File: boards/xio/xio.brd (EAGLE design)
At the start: 170 x 100 mm, 146 parts, among them Y2 NX3225SA-12.000MHZ-STD-CSR-1

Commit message: Latest snapshot
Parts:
- removed C36, C51: 0.1uF, rcl:C0402K
- removed ECI: eci, microbuilder:2X23
- removed XIO: STM32H753B-XIO, sjg-stm32:PQFP208
- added JP1: (no value), pinhead:1X04
- added JP2, JP3: (no value), pinhead:2X06
- added TP1, TP2, TP3, TP4: (no value), microbuilder:TESTPOINT_ROUND_1MM
- added U$2: A8_CART, sjg-con:A8_CART
- added U$3: XIO, sjg-stm32:PQFP208
- moved ARCH_ID 147.5 mm to (152.6, 92.3), turned to 0 degrees
- moved R6 142.0 mm to (156.6, 85.9)
- moved R7 139.9 mm to (154.0, 85.9)
- moved PID 139.0 mm to (140.0, 92.5), turned to 0 degrees
- moved R8 137.9 mm to (151.5, 85.9)
- moved R9 135.9 mm to (149.0, 85.9)
- moved MEM_ID 133.5 mm to (129.9, 92.7), turned to 0 degrees
- moved R14 131.3 mm to (142.4, 86.0)
- moved R15 129.6 mm to (139.9, 86.0)
- moved R16 127.9 mm to (137.3, 86.0)
- moved R17 125.3 mm to (132.1, 86.1)
- moved R18 122.8 mm to (128.3, 86.1)
- moved C35 96.3 mm to (142.6, 15.2), turned to 180 degrees
- moved XIO-SWD 69.2 mm to (4.11, 26.5), turned to 270 degrees
- moved R89 64.2 mm to (8.68, 25.4), turned to 270 degrees
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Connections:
- removed net I2C_SCL: SLOT0.B42, SLOT1.B42, SLOT2.B42, SLOT3.B42, SLOT4.B42, XIO.91
- removed net I2C_SDA: SLOT0.B43, SLOT1.B43, SLOT2.B43, SLOT3.B43, SLOT4.B43, XIO.90
- new net AUX_CTS: JP1.1, SLOT0.B46, SLOT1.B46, SLOT2.B46, SLOT3.B46, SLOT4.B46, U$3.30
- new net AUX_RTS: JP1.4, SLOT0.B47, SLOT1.B47, SLOT2.B47, SLOT3.B47, SLOT4.B47, U$3.29
- new net AUX_RX: JP1.2, SLOT0.B48, SLOT1.B48, SLOT2.B48, SLOT3.B48, SLOT4.B48, U$3.27
- new net AUX_TX: JP1.3, SLOT0.B49, SLOT1.B49, SLOT2.B49, SLOT3.B49, SLOT4.B49, U$3.28
- new net N$3: TP1.P$1, U$3.134
- new net N$4: TP2.P$1, U$3.178
- new net N$5: TP3.P$1, U$3.102
- new net N$6: TP4.P$1, U$3.175
- new net USRA_CLK: JP2.1, U$3.45
- new net USRA_D0: JP2.3, U$3.35
- new net USRA_D1: JP2.4, U$3.36
- new net USRA_D2: JP2.5, U$3.37
- new net USRA_D3: JP2.6, U$3.38
- new net USRA_D4: JP2.7, U$3.57
- new net USRA_D5: JP2.8, U$3.58
- new net USRA_D6: JP2.9, U$3.138
- new net USRA_D7: JP2.10, U$3.139
- new net USRA_MISC: JP2.11, U$3.10
- new net USRB_CLK: JP3.1, U$3.130
- new net USRB_D0: JP3.3, U$3.126
- new net USRB_D1: JP3.4, U$3.127
- new net USRB_D2: JP3.5, U$3.128
- new net USRB_D3: JP3.6, U$3.186
- new net USRB_D4: JP3.7, U$3.187
- new net USRB_D5: JP3.8, U$3.188
- new net USRB_D6: JP3.9, U$3.189
- new net USRB_D7: JP3.10, U$3.190
- new net USRB_MISC: JP3.11, U$3.177
- net !RESET!: now also U$3.34; no longer XIO.34
- net !VHDCI_EXSEL!: now also U$3.68; no longer ECI.1, XIO.68
- net !VHDCI_IRQ!: now also U$3.69; no longer ECI.2, XIO.69
- net !VHDCI_MPD!: now also U$3.67; no longer ECI.3, XIO.67
- net +3V3: now also JP2.2, JP3.2, U$3.103, U$3.115, U$3.124, U$3.137, U$3.15, U$3.150, U$3.158, U$3.171, U$3.185, U$3.204, U$3.26, U$3.39, U$3.52, U$3.59, U$3.6, U$3.73, U$3.83, U$3.94; no longer XIO.103, XIO.115, XIO.124, XIO.137, XIO.15, XIO.150, XIO.158, XIO.171, XIO.185, XIO.204, XIO.26, XIO.39, XIO.52, XIO.59, XIO.6, XIO.73, XIO.83, XIO.94
- net +5V: now also U$2.P13; no longer C36.1, C51.1, ECI.42, ECI.44, ECI.46
- net ARCH0: now also U$3.96
- net ARCH1: now also U$3.97
- net ARCH2: now also U$3.98
- net ARCH3: now also U$3.99
- net A_OK: now also U$3.176
- net GND: now also JP2.12, JP3.12, U$2.PB, U$3.114, U$3.125, U$3.136, U$3.14, U$3.149, U$3.170, U$3.184, U$3.202, U$3.25, U$3.40, U$3.51, U$3.60, U$3.72, U$3.82, U$3.93; no longer C36.2, C51.2, ECI.41, ECI.43, ECI.45, SLOT0.B41, SLOT0.B44, SLOT1.B41, SLOT1.B44, SLOT2.B41, SLOT2.B44, SLOT3.B41, SLOT3.B44, SLOT4.B41, SLOT4.B44, XIO.114, XIO.125, XIO.136, XIO.14, XIO.149, XIO.170, XIO.184, XIO.202, XIO.25, XIO.40, XIO.51, XIO.60, XIO.72, XIO.82, XIO.93
- net MEM0: now also U$3.100
- net MEM1: now also U$3.101
- net N$1: now also U$3.33; no longer XIO.33
- net N$107: now also U$3.9; no longer XIO.192
- net N$108: now also U$3.111; no longer XIO.193
- net N$109: now also U$3.112; no longer XIO.104
- net N$11: now also U$3.197; no longer XIO.197
- net N$110: now also U$3.113; no longer XIO.31
- net N$111: now also U$3.31; no longer XIO.179
- net N$112: now also U$3.133; no longer XIO.180
- net N$13: now also U$3.46; no longer XIO.169
- net N$14: now also U$3.47; no longer XIO.172
- net N$15: now also U$3.48; no longer XIO.173
- net N$2: now also U$3.32; no longer XIO.32
- net N$34: now also U$3.167; no longer XIO.43
- net N$35: now also U$3.172; no longer XIO.50
- net N$39: now also U$3.169; no longer XIO.45
- net N$40: now also U$3.168; no longer XIO.44
- net N$57: now also U$3.54; no longer XIO.105
- net N$61: now also U$3.56; no longer XIO.107
- net N$64: now also U$3.160; no longer XIO.160
- net N$65: now also U$3.53; no longer XIO.199
- net N$7: now also U$3.203; no longer XIO.203
- net N$86: now also U$3.50; no longer XIO.61
- net N$93: now also U$3.8; no longer XIO.63
- net PID0: now also U$3.151
- net PID1: now also U$3.152
- net PID2: now also U$3.153
- net SD0: now also U$3.140
- net SD1: now also U$3.141
- net SD2: now also U$3.161
- net SD3: now also U$3.162
- net SDCD: now also U$3.173
- net SDCLK: now also U$3.163
- net SDCMD: now also U$3.166
- net SPI_CLK: now also SLOT0.B41, SLOT1.B41, SLOT2.B41, SLOT3.B41, SLOT4.B41; no longer SLOT0.B45, SLOT1.B45, SLOT2.B45, SLOT3.B45, SLOT4.B45
- net SPI_IRQ0: now also SLOT0.B42, U$3.179; no longer SLOT0.B48, XIO.99
- net SPI_IRQ1: now also SLOT1.B42, U$3.180; no longer SLOT1.B48, XIO.100
- net SPI_IRQ2: now also SLOT2.B42, U$3.181; no longer SLOT2.B48, XIO.101
- net SPI_IRQ3: now also SLOT3.B42, U$3.182; no longer SLOT3.B48, XIO.102
- net SPI_IRQ4: now also SLOT4.B42, U$3.183; no longer SLOT4.B48
- net SPI_MISO: now also SLOT0.B43, SLOT1.B43, SLOT2.B43, SLOT3.B43, SLOT4.B43, U$3.55; no longer SLOT0.B46, SLOT1.B46, SLOT2.B46, SLOT3.B46, SLOT4.B46, XIO.106
- net SPI_MOSI: now also SLOT0.B44, SLOT1.B44, SLOT2.B44, SLOT3.B44, SLOT4.B44; no longer SLOT0.B47, SLOT1.B47, SLOT2.B47, SLOT3.B47, SLOT4.B47
- net SPI_SS0: now also SLOT0.B45, U$3.1; no longer SLOT0.B49, XIO.46
- net SPI_SS1: now also SLOT1.B45, U$3.2; no longer SLOT1.B49, XIO.47
- net SPI_SS2: now also SLOT2.B45, U$3.3; no longer SLOT2.B49, XIO.48
- net SPI_SS3: now also SLOT3.B45, U$3.4; no longer SLOT3.B49, XIO.130
- net SPI_SS4: now also SLOT4.B45, U$3.5; no longer SLOT4.B49, XIO.96
- net VHDCI_A0: now also U$2.P5, U$3.107; no longer ECI.5, XIO.35
- net VHDCI_A1: now also U$2.P4, U$3.106; no longer ECI.6, XIO.36
- net VHDCI_A10: now also U$2.PP, U$3.194; no longer ECI.15, XIO.161
- net VHDCI_A11: now also U$2.PN, U$3.193; no longer ECI.16, XIO.162
- net VHDCI_A12: now also U$2.PK, U$3.192; no longer ECI.17, XIO.163
- net VHDCI_A13: now also U$3.63; no longer ECI.18, XIO.8
- net VHDCI_A14: now also U$3.62; no longer ECI.19, XIO.9
- net VHDCI_A15: now also U$3.61; no longer ECI.20, XIO.10
- net VHDCI_A2: now also U$2.P3, U$3.105; no longer ECI.7, XIO.37
- net VHDCI_A3: now also U$2.P2, U$3.104; no longer ECI.8, XIO.38
- net VHDCI_A4: now also U$2.PC, U$3.91; no longer ECI.9, XIO.57
- net VHDCI_A5: now also U$2.PD, U$3.90; no longer ECI.10, XIO.58
- net VHDCI_A6: now also U$2.PE, U$3.199; no longer ECI.11, XIO.138
- net VHDCI_A7: now also U$2.PF, U$3.198; no longer ECI.12, XIO.139
- net VHDCI_A8: now also U$2.PH, U$3.196; no longer ECI.13, XIO.140
- net VHDCI_A9: now also U$2.PJ, U$3.195; no longer ECI.14, XIO.141
- net VHDCI_AUDIO_SIO: no longer ECI.4
- net VHDCI_CCTL: now also U$2.P15, U$3.95; no longer ECI.21, XIO.95
- net VHDCI_CLK: now also U$2.PS, U$3.65; no longer ECI.22, XIO.65
- net VHDCI_D0: now also U$2.P10, U$3.154; no longer ECI.24, XIO.154
- net VHDCI_D1: now also U$2.P9, U$3.155; no longer ECI.25, XIO.155
- net VHDCI_D1XX: now also U$3.121; no longer ECI.23, XIO.121
- net VHDCI_D2: now also U$2.P8, U$3.156; no longer ECI.26, XIO.156
- net VHDCI_D3: now also U$2.PL, U$3.157; no longer ECI.27, XIO.157
- net VHDCI_D4: now also U$2.P6, U$3.205; no longer ECI.28, XIO.205
- net VHDCI_D5: now also U$2.P7, U$3.206; no longer ECI.29, XIO.206
- net VHDCI_D6: now also U$2.P11, U$3.207; no longer ECI.30, XIO.207
- net VHDCI_D7: now also U$2.PM, U$3.208; no longer ECI.31, XIO.208
- net VHDCI_GND: no longer ECI.32
- net VHDCI_HALT: now also U$3.123; no longer ECI.33, XIO.123
- net VHDCI_RD4: now also U$2.PA, U$3.66; no longer ECI.34, XIO.66
- net VHDCI_RD5: now also U$2.P14, U$3.64; no longer ECI.35, XIO.64
- net VHDCI_REF: now also U$3.120; no longer ECI.36, XIO.120
- net VHDCI_RSRVD0: now also U$3.7; no longer XIO.7
- net VHDCI_RSRVD1: now also U$3.11; no longer XIO.11
- net VHDCI_RSRVD2: now also U$3.12; no longer XIO.12
- net VHDCI_RSRVD3: now also U$3.13; no longer XIO.13
- net VHDCI_RSRVD4: now also U$3.19; no longer XIO.19
- net VHDCI_RSRVD5: now also U$3.20; no longer XIO.20
- net VHDCI_RSRVD6: now also U$3.21; no longer XIO.21
- net VHDCI_RST: now also U$3.122; no longer ECI.37, XIO.122
- net VHDCI_RW: now also U$2.PR, U$3.174; no longer ECI.38, XIO.174
- net VHDCI_S4: now also U$2.P1, U$3.119; no longer ECI.39, XIO.119
- net VHDCI_S5: now also U$2.P12, U$3.118; no longer ECI.40, XIO.118
- net XIO_RAM_A0: now also U$3.16; no longer XIO.16
- net XIO_RAM_A1: now also U$3.17; no longer XIO.17
- net XIO_RAM_A10: now also U$3.77; no longer XIO.77
- net XIO_RAM_A11: now also U$3.78; no longer XIO.78
- net XIO_RAM_A12: now also U$3.129; no longer XIO.129
- net XIO_RAM_A2: now also U$3.18; no longer XIO.18
- net XIO_RAM_A3: now also U$3.22; no longer XIO.22
- net XIO_RAM_A4: now also U$3.23; no longer XIO.23
- net XIO_RAM_A5: now also U$3.24; no longer XIO.24
- net XIO_RAM_A6: now also U$3.71; no longer XIO.71
- net XIO_RAM_A7: now also U$3.74; no longer XIO.74
- net XIO_RAM_A8: now also U$3.75; no longer XIO.75
- net XIO_RAM_A9: now also U$3.76; no longer XIO.76
- net XIO_RAM_BA0: now also U$3.131; no longer XIO.131
- net XIO_RAM_BA1: now also U$3.132; no longer XIO.132
- net XIO_RAM_CAS: now also U$3.191; no longer XIO.191
- net XIO_RAM_CLK: now also U$3.135; no longer XIO.135
- net XIO_RAM_D0: now also U$3.116; no longer XIO.116
- net XIO_RAM_D1: now also U$3.117; no longer XIO.117
- net XIO_RAM_D10: now also U$3.87; no longer XIO.87
- net XIO_RAM_D11: now also U$3.88; no longer XIO.88
- net XIO_RAM_D12: now also U$3.89; no longer XIO.89
- net XIO_RAM_D13: now also U$3.108; no longer XIO.108
- net XIO_RAM_D14: now also U$3.109; no longer XIO.109
- net XIO_RAM_D15: now also U$3.110; no longer XIO.110
- net XIO_RAM_D2: now also U$3.164; no longer XIO.164
- net XIO_RAM_D3: now also U$3.165; no longer XIO.165
- net XIO_RAM_D4: now also U$3.79; no longer XIO.79
- net XIO_RAM_D5: now also U$3.80; no longer XIO.80
- net XIO_RAM_D6: now also U$3.81; no longer XIO.81
- net XIO_RAM_D7: now also U$3.84; no longer XIO.84
- net XIO_RAM_D8: now also U$3.85; no longer XIO.85
- net XIO_RAM_D9: now also U$3.86; no longer XIO.86
- net XIO_RAM_DQMH: now also U$3.201; no longer XIO.201
- net XIO_RAM_DQML: now also U$3.200; no longer XIO.200
- net XIO_RAM_RAS: now also U$3.70; no longer XIO.70
- net XIO_RAM_WE: now also U$3.49; no longer XIO.49
- net XIO_RX: now also U$3.44; no longer XIO.196
- net XIO_SWDCLK: now also U$3.159; no longer XIO.159
- net XIO_SWDIO: now also U$3.147; no longer XIO.147
- net XIO_TX: now also U$3.43; no longer XIO.195
- net XIO_USB_N: now also U$3.145; no longer XIO.145
- net XIO_USB_P: now also U$3.146; no longer XIO.146
- net XIO_VCAP1: now also U$3.92; no longer XIO.92
- net XIO_VCAP2: now also U$3.148; no longer XIO.148
- net XIO_VDDA: now also U$3.41, U$3.42; no longer XIO.41, XIO.42
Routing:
- net GND: track 0.00 -> 467.5 mm, vias 0 -> 33
- net VHDCI_RW: track 0.00 -> 402.0 mm, vias 0 -> 13
- net VHDCI_S5: track 0.00 -> 388.4 mm, vias 0 -> 13
- net +5V: track 0.00 -> 369.2 mm, vias 0 -> 64
- net VHDCI_D4: track 0.00 -> 342.4 mm, vias 0 -> 10
- net VHDCI_D3: track 0.00 -> 331.5 mm, vias 0 -> 5
- net VHDCI_RD5: track 0.00 -> 325.1 mm, vias 0 -> 8
- net VHDCI_REF: track 0.00 -> 315.5 mm, vias 0 -> 12
- net ARCH2: track 0.00 -> 311.7 mm, vias 0 -> 8
- net VHDCI_D1: track 0.00 -> 309.7 mm, vias 0 -> 7
- net VHDCI_A7: track 0.00 -> 296.4 mm, vias 0 -> 11
- net VHDCI_S4: track 0.00 -> 294.4 mm, vias 0 -> 10
- net VHDCI_CLK: track 0.00 -> 290.0 mm, vias 0 -> 11
- net VHDCI_D0: track 0.00 -> 287.8 mm, vias 0 -> 8
- net VHDCI_D2: track 0.00 -> 287.3 mm, vias 0 -> 9
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- added copper zone on layer 15, net +3V3
- added copper zone on layer 15, net +5V
- added copper zone on layer 2, net GND
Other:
- board text added: "Indent SD card slot Make parts for STM32F Neaten everything up Add 5v plane rectangle Add GND plane Add 3.3v plane"
- board text removed: "Indent SD card slot Make parts for STM32F Neaten everything up Make cartridge part 5650118-1 and place Add 5v plane rectangle Add GND plane Add 3.3v plane Find better (larger) USB ESD part"

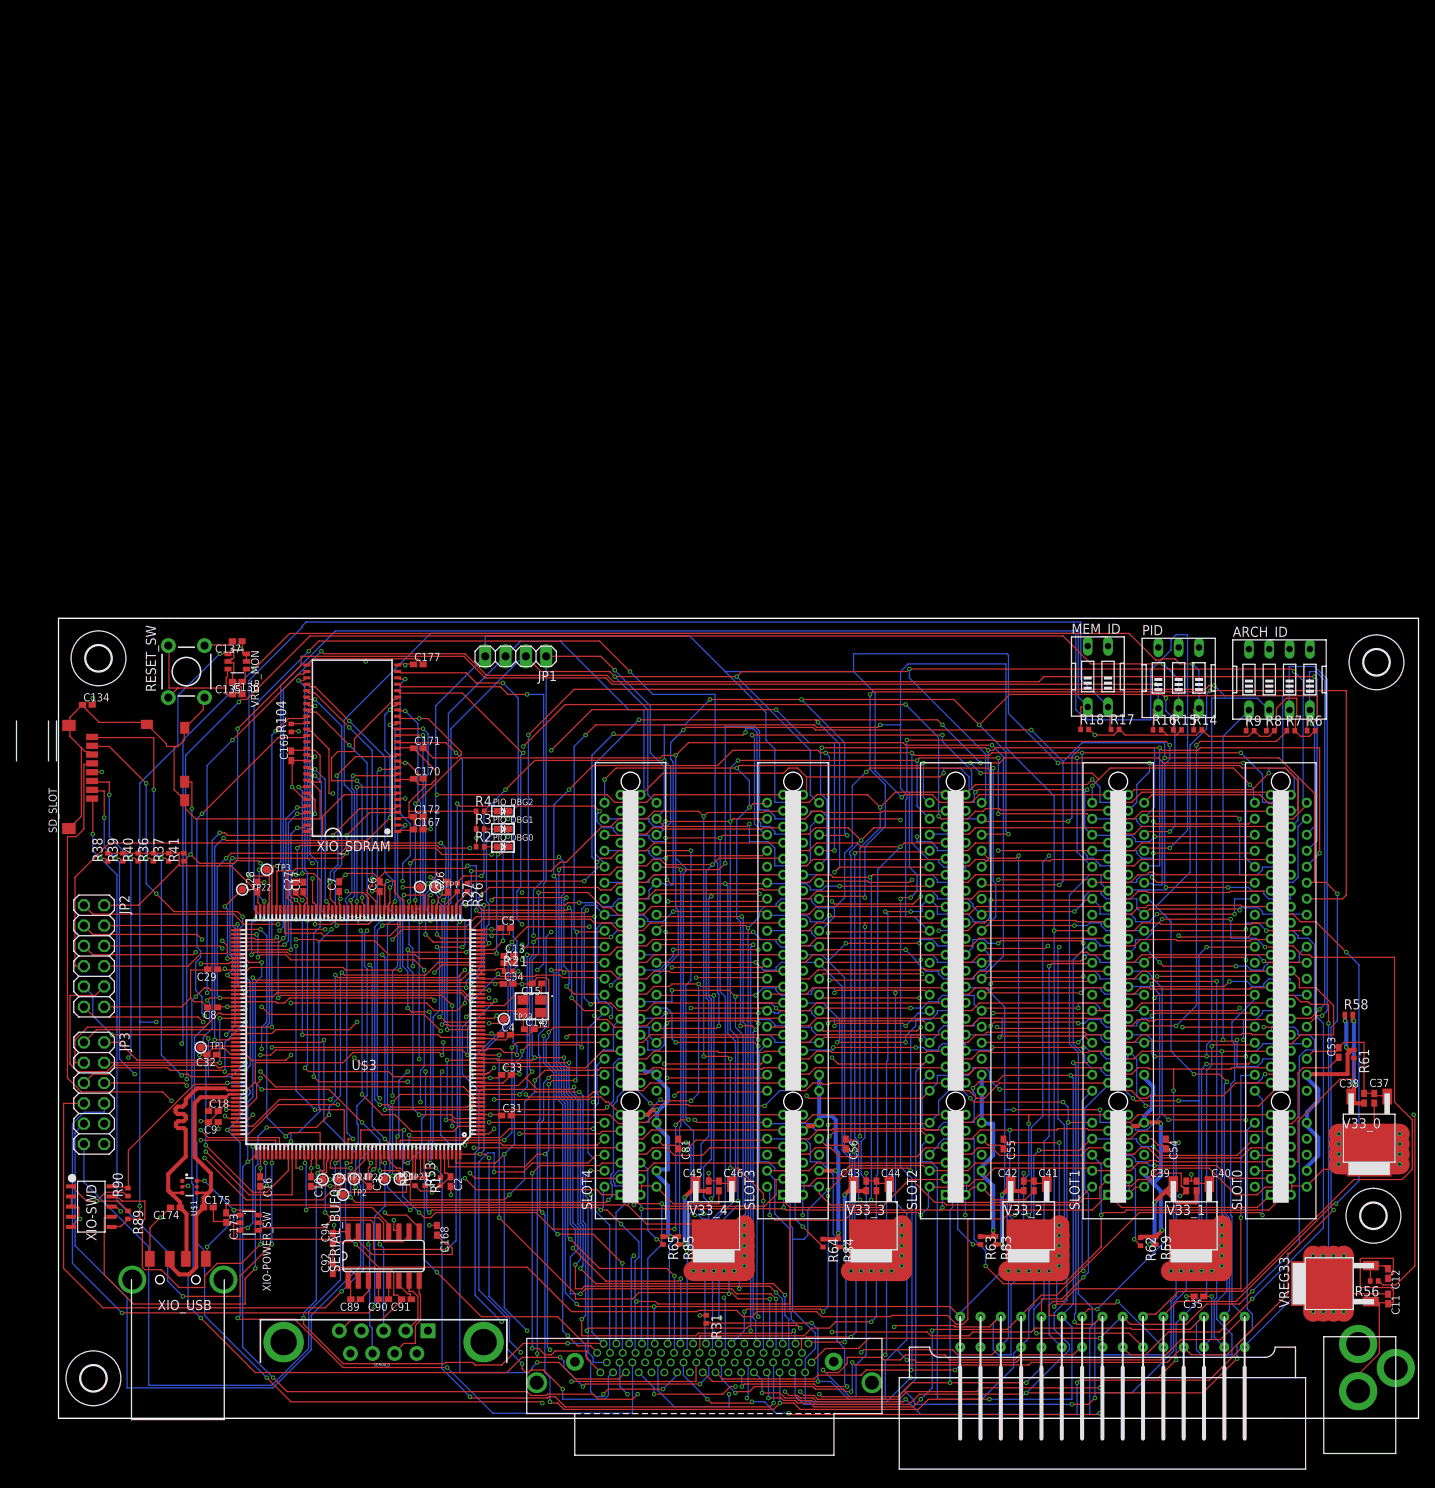
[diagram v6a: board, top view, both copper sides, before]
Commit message: Routed single-cpu board  - no CPLD on-board as yet.
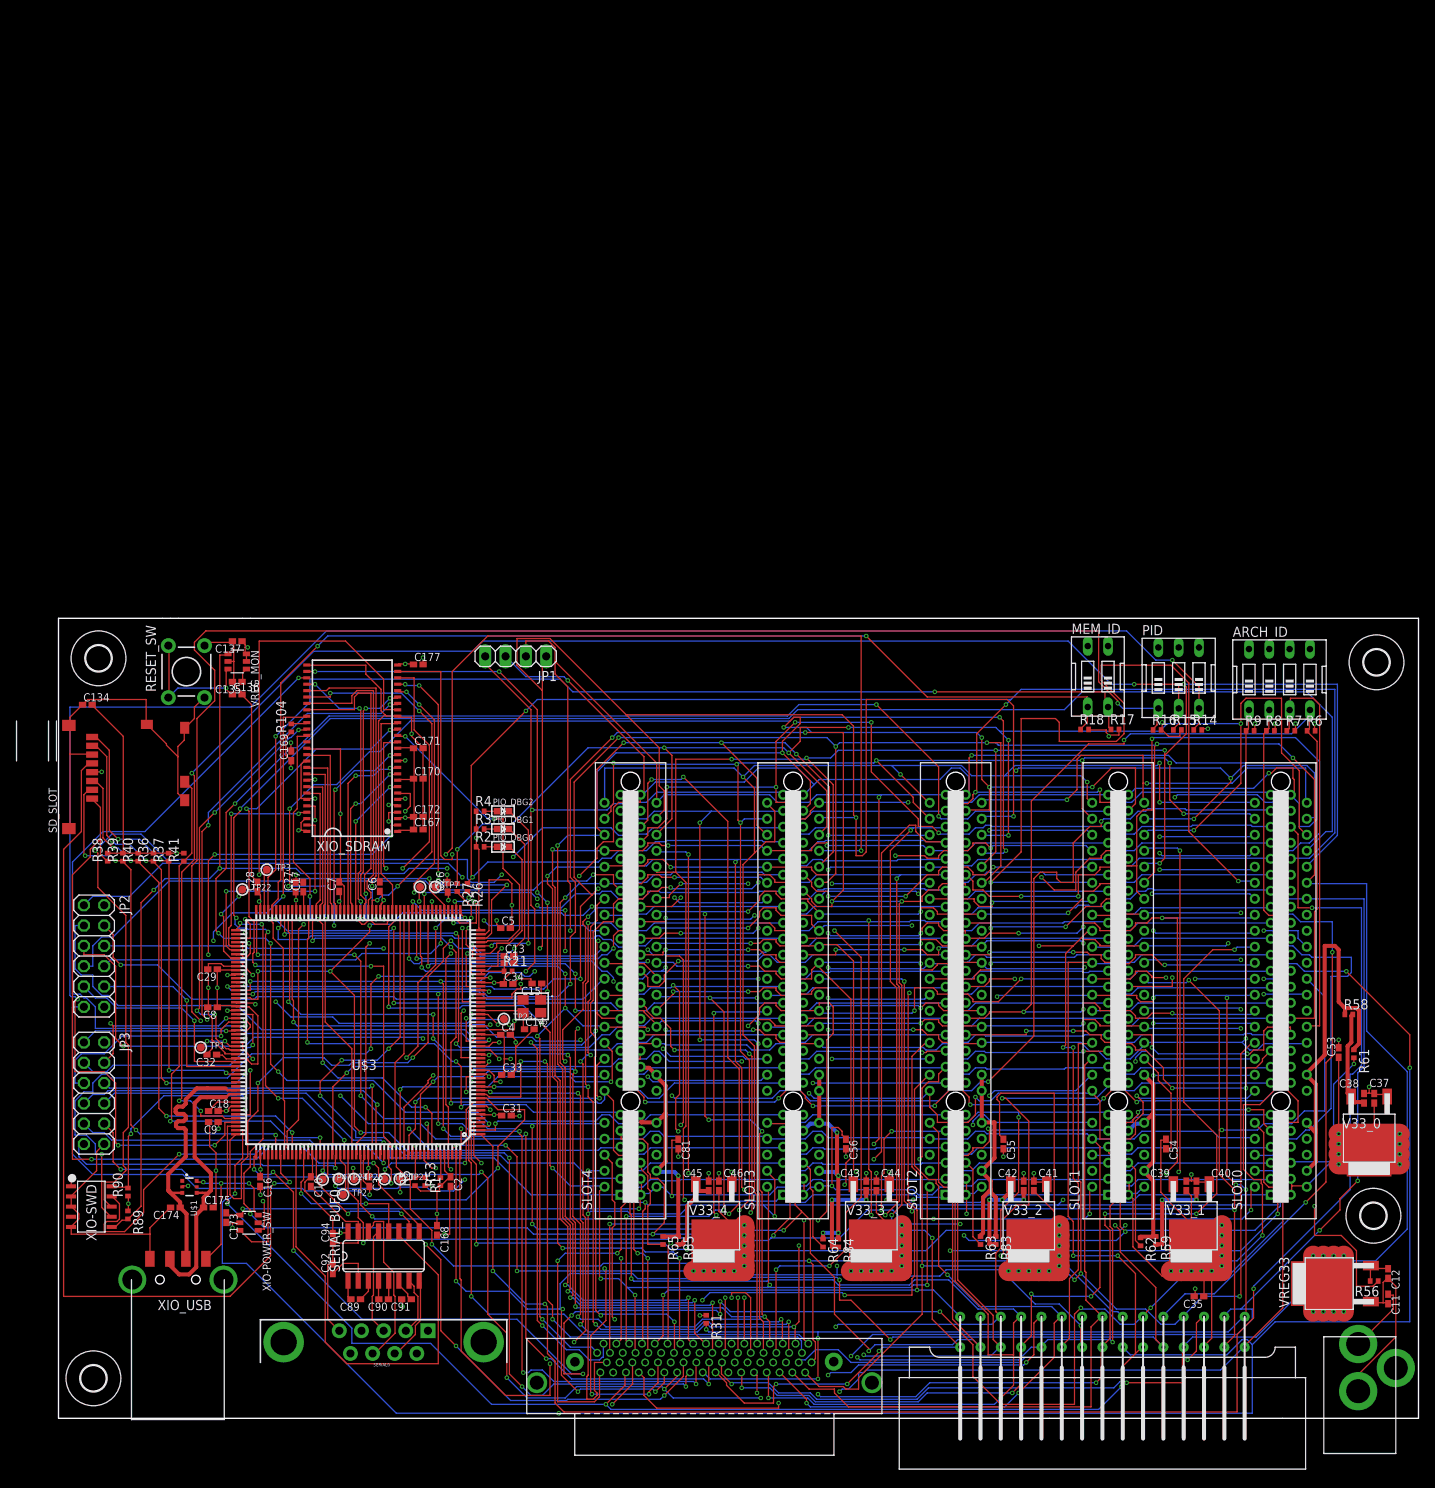
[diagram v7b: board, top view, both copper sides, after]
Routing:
- net ARCH2: track 311.7 -> 197.1 mm, vias 8 -> 6
- net VHDCI_D4: track 342.4 -> 233.9 mm, vias 10 -> 7
- net SPI_CLK: track 145.3 -> 245.9 mm, vias 4 -> 6
- net VHDCI_J1_A1: track 146.4 -> 234.7 mm, vias 6 -> 8
- net VHDCI_REF: track 315.5 -> 227.7 mm, vias 12 -> 9
- net VHDCI_SIO_CLK_IN: track 258.0 -> 170.6 mm
- net VHDCI_A7: track 296.4 -> 210.1 mm, vias 11 -> 7
- net VHDCI_J1_1: track 247.0 -> 166.2 mm, vias 10 -> 8
- net VHDCI_A2: track 222.7 -> 295.5 mm, vias 6 -> 12
- net VHDCI_RD4: track 279.7 -> 209.3 mm, vias 11 -> 7
- net VHDCI_A9: track 272.3 -> 208.3 mm, vias 10 -> 5
- net GND: track 467.5 -> 405.2 mm, vias 33 -> 56
- net AUX_RX: track 252.3 -> 190.9 mm, vias 5 -> 6
- net AUX_RTS: track 261.0 -> 201.1 mm, vias 5 -> 9
- net XIO_TX: track 60.1 -> 118.6 mm, vias 2 -> 3
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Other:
- board text added: "Indent SD card slot Check serial tx/rx lines"
- board text removed: "Indent SD card slot Make parts for STM32F Neaten everything up Add 5v plane rectangle Add GND plane Add 3.3v plane"
